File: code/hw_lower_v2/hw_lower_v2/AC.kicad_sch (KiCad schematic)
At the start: 39 parts, among them K1 AHES4191, Q1 BSS138, Q2 BSS138, Q3 BSS138, T1 TS3193-2C 2mA/2mA, U1 BRCS02C, U2 BL0942

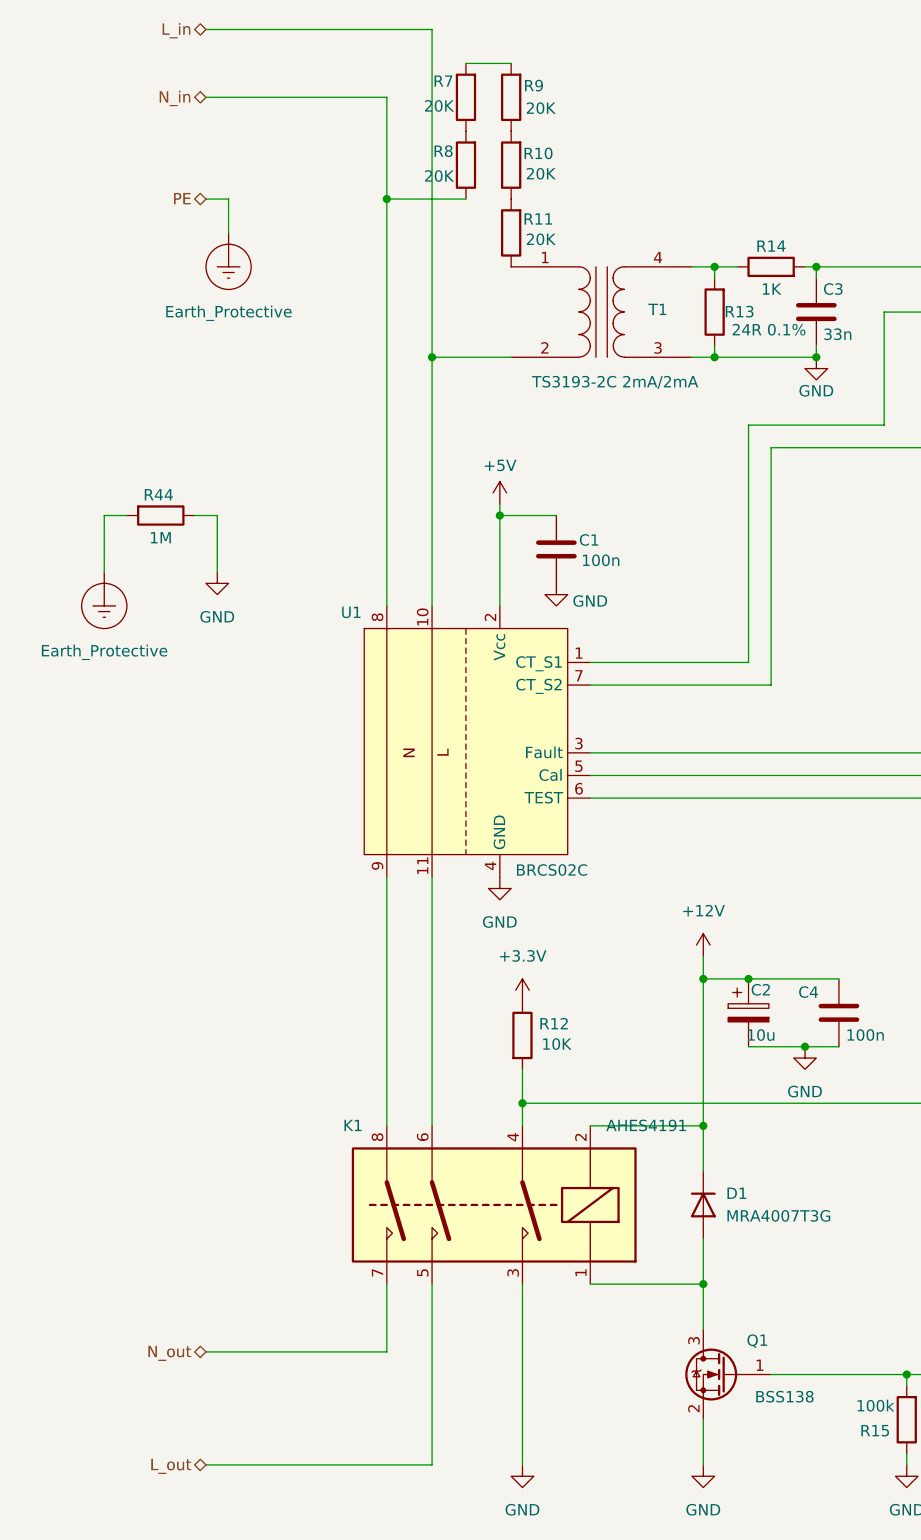
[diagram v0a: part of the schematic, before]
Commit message: further placement and pin relocation
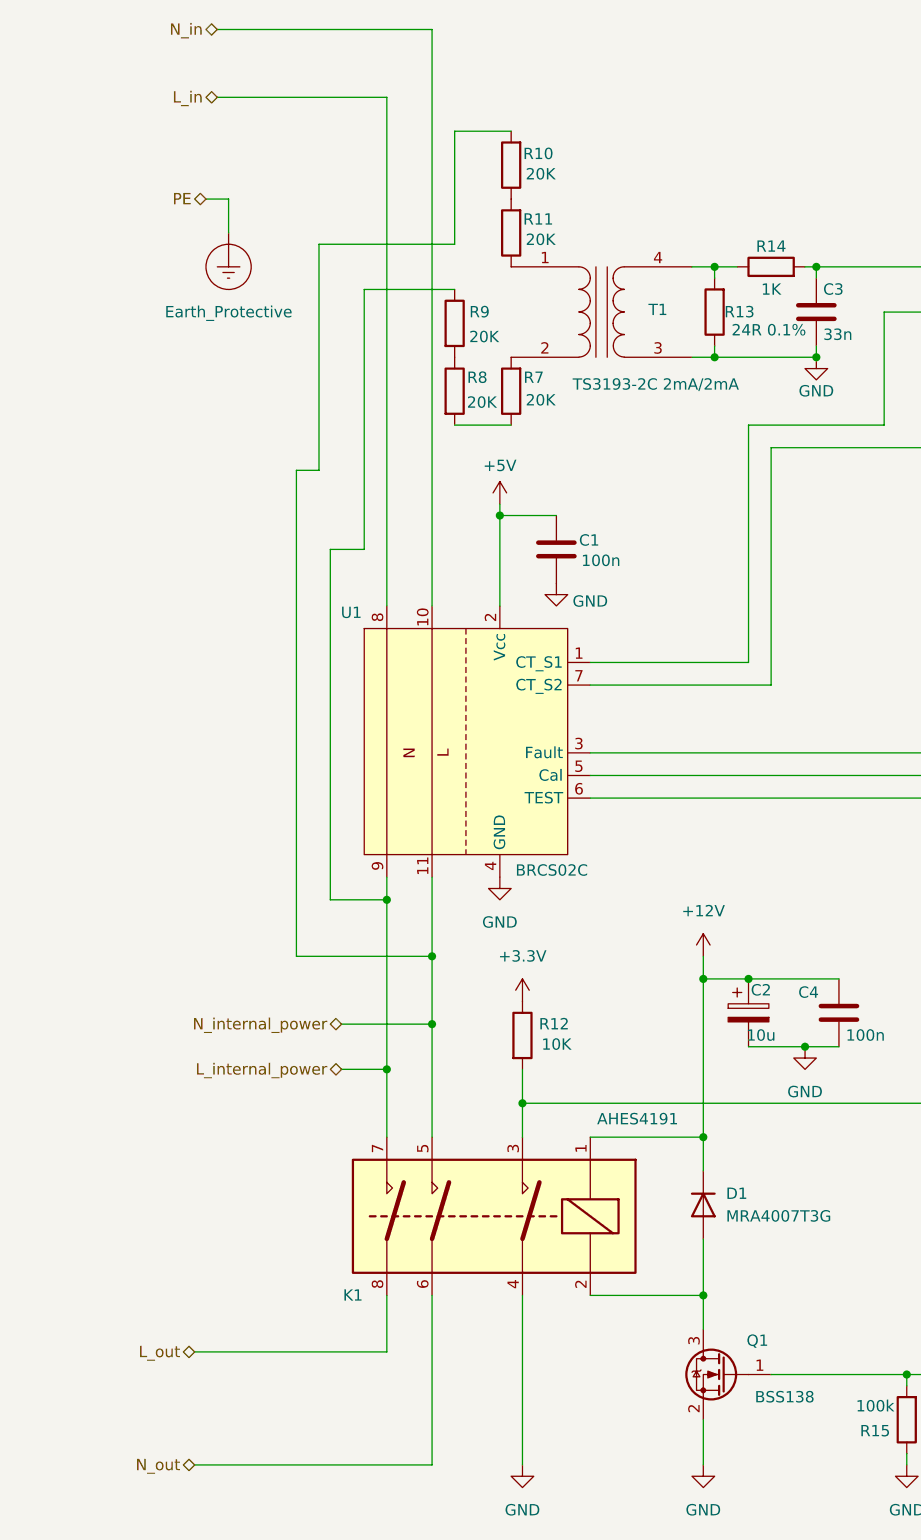
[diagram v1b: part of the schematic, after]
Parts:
- removed R44: 1M, Resistor_SMD:R_1206_3216Metric, symbol Device:R
- U1: footprint multi_new:BRCS02C_1 -> multi_new:BRCS02C_2
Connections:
- net +12V: now also K1.1; no longer K1.2
- net AC_RELAY_SENSE: now also K1.3; no longer K1.4
- net GND: now also K1.4; no longer K1.3
- net L_in: now also U1.8; no longer T1.2 (AB), U1.10
- net L_out: now also K1.8; no longer K1.5
- net N_in: now also U1.10; no longer R8.1, U1.8
- net N_out: now also K1.6; no longer K1.7
- net at R9.2: now also R8.1; no longer R7.2
- net at D1.2 (A), Q1.3 (D): now also K1.2; no longer K1.1
- net N_internal_power: now reaches U1.11
- net N_internal_power: now also K1.5, R10.2; no longer K1.6
- net L_internal_power: now reaches U1.9
- net L_internal_power: now also K1.7, R9.1; no longer K1.8
- new net: R7.2, T1.2 (AB)
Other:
- moved on the sheet: K1, R7, R8, R9

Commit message: commit before experimenting
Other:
- moved on the sheet: C1, C3, C5, C6, C7, Q2, Q3, R10, R11, R13, R14, R16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

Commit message: have one project part library
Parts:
- U2: footprint JLCPCB:SSOP-10_L4.9-W3.9-P1.00-LS6.0-BL -> multi_new:SSOP-10_L4.9-W3.9-P1.00-LS6.0-BL

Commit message: right before tracks
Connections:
- net L_in: now also U1.10; no longer U1.8
- net L_internal_power: now also K1.5, R10.2, U1.11; no longer K1.7, R9.1, U1.9
- net L_out: now also K1.6; no longer K1.8
- net N_in: now also U1.8; no longer U1.10
- net N_internal_power: now also K1.7, R9.1, U1.9; no longer K1.5, R10.2, U1.11
- net N_out: now also K1.8; no longer K1.6

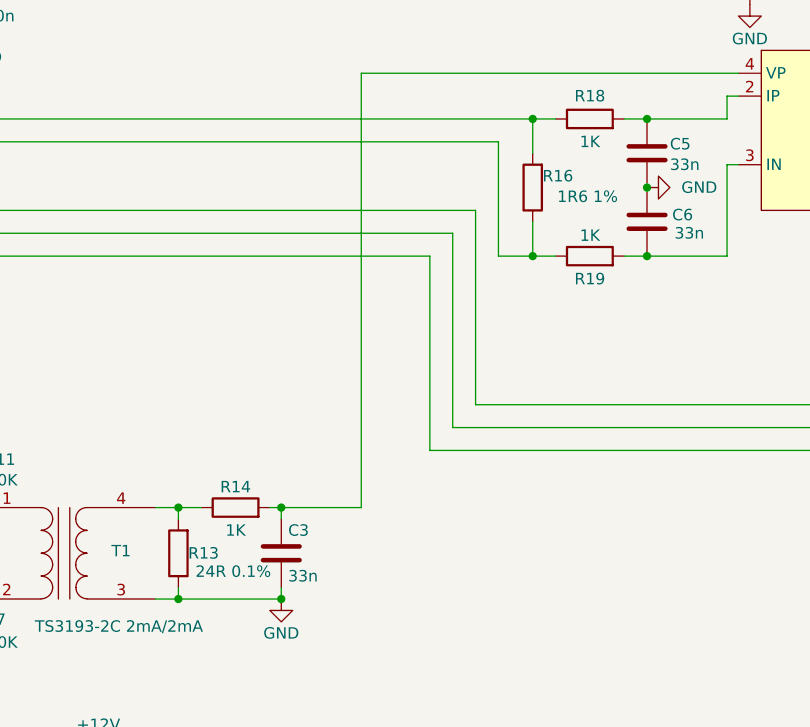
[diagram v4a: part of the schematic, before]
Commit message: moved stuff around a little bit, will optimise the number of components now
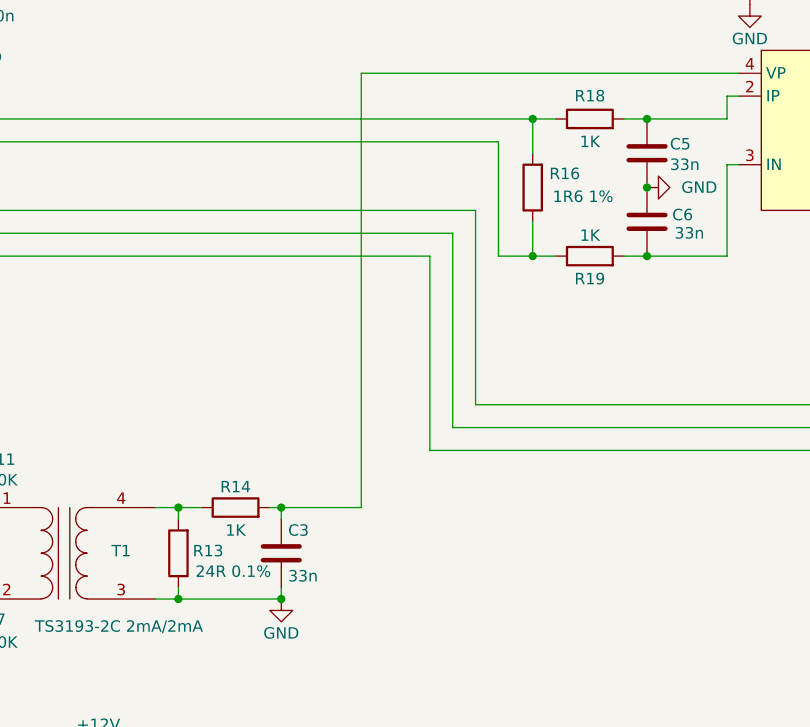
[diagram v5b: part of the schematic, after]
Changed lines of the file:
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@@
 		(dnp no)
 		(property "Reference" "R13"
-			(at 108.204 102.87 0)
+			(at 108.712 102.616 0)
 			(effects
 				(font
@@
 		(dnp no)
 		(property "Reference" "R16"
-			(at 147.574 60.96 0)
+			(at 148.336 60.706 0)
 			(effects
 				(font
@@
 		)
 		(property "Value" "1R6 1%"
-			(at 150.876 63.246 0)
-			(effects
-				(font
+			(at 150.368 63.246 0)
+			(effects
+				(font

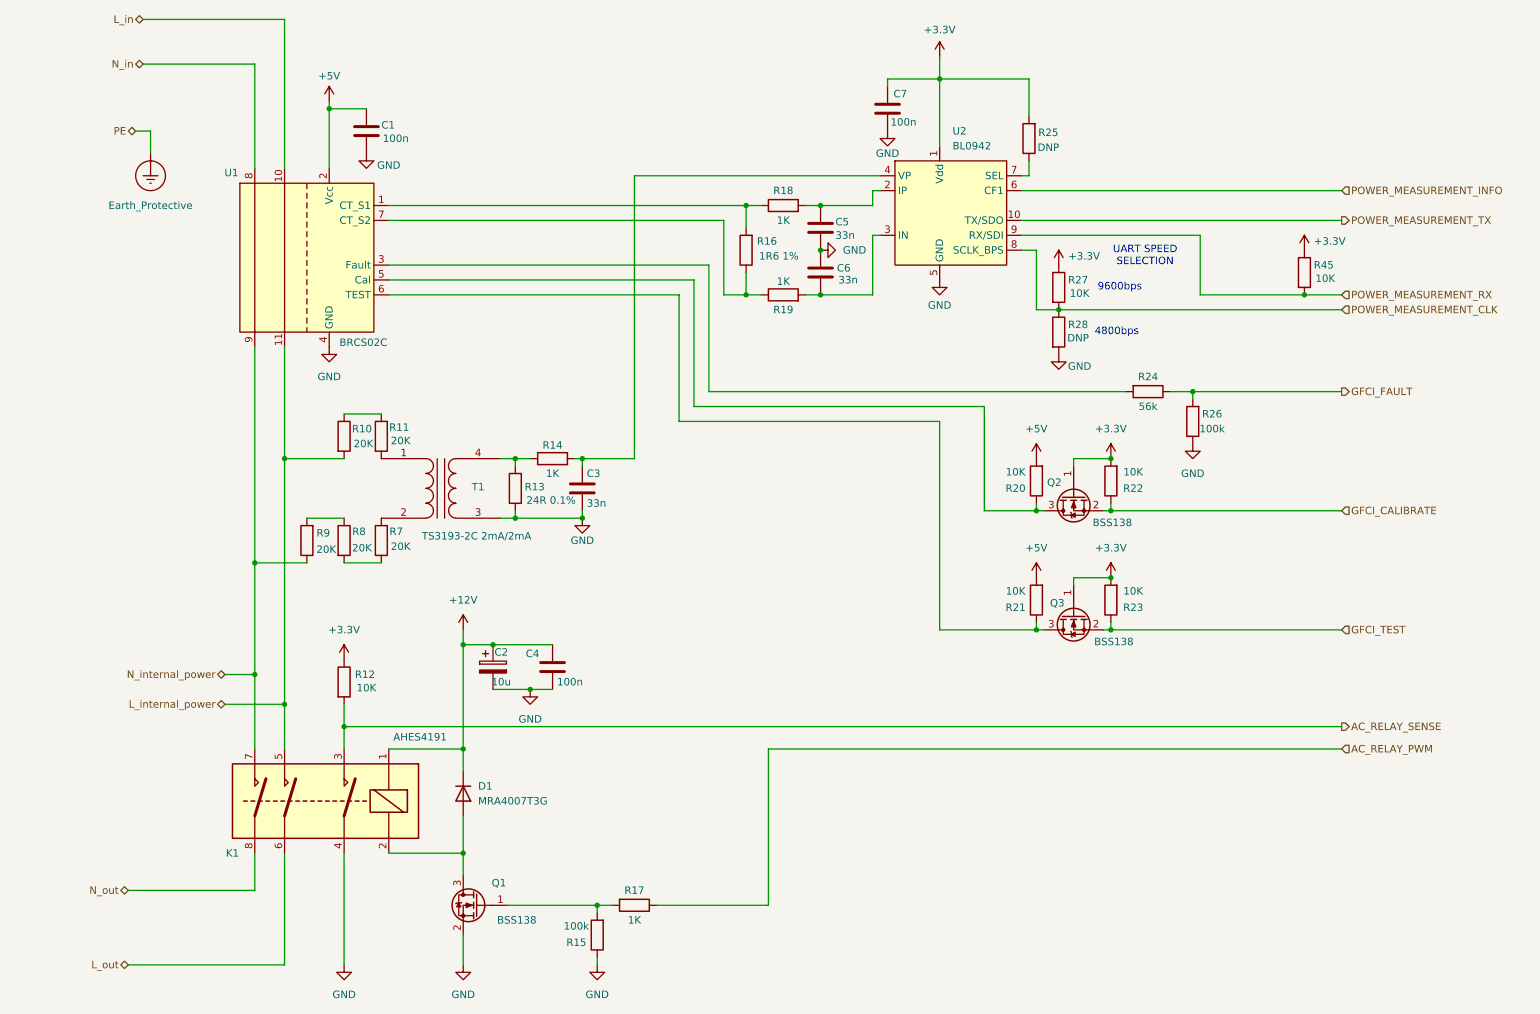
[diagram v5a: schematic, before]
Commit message: simplify component values
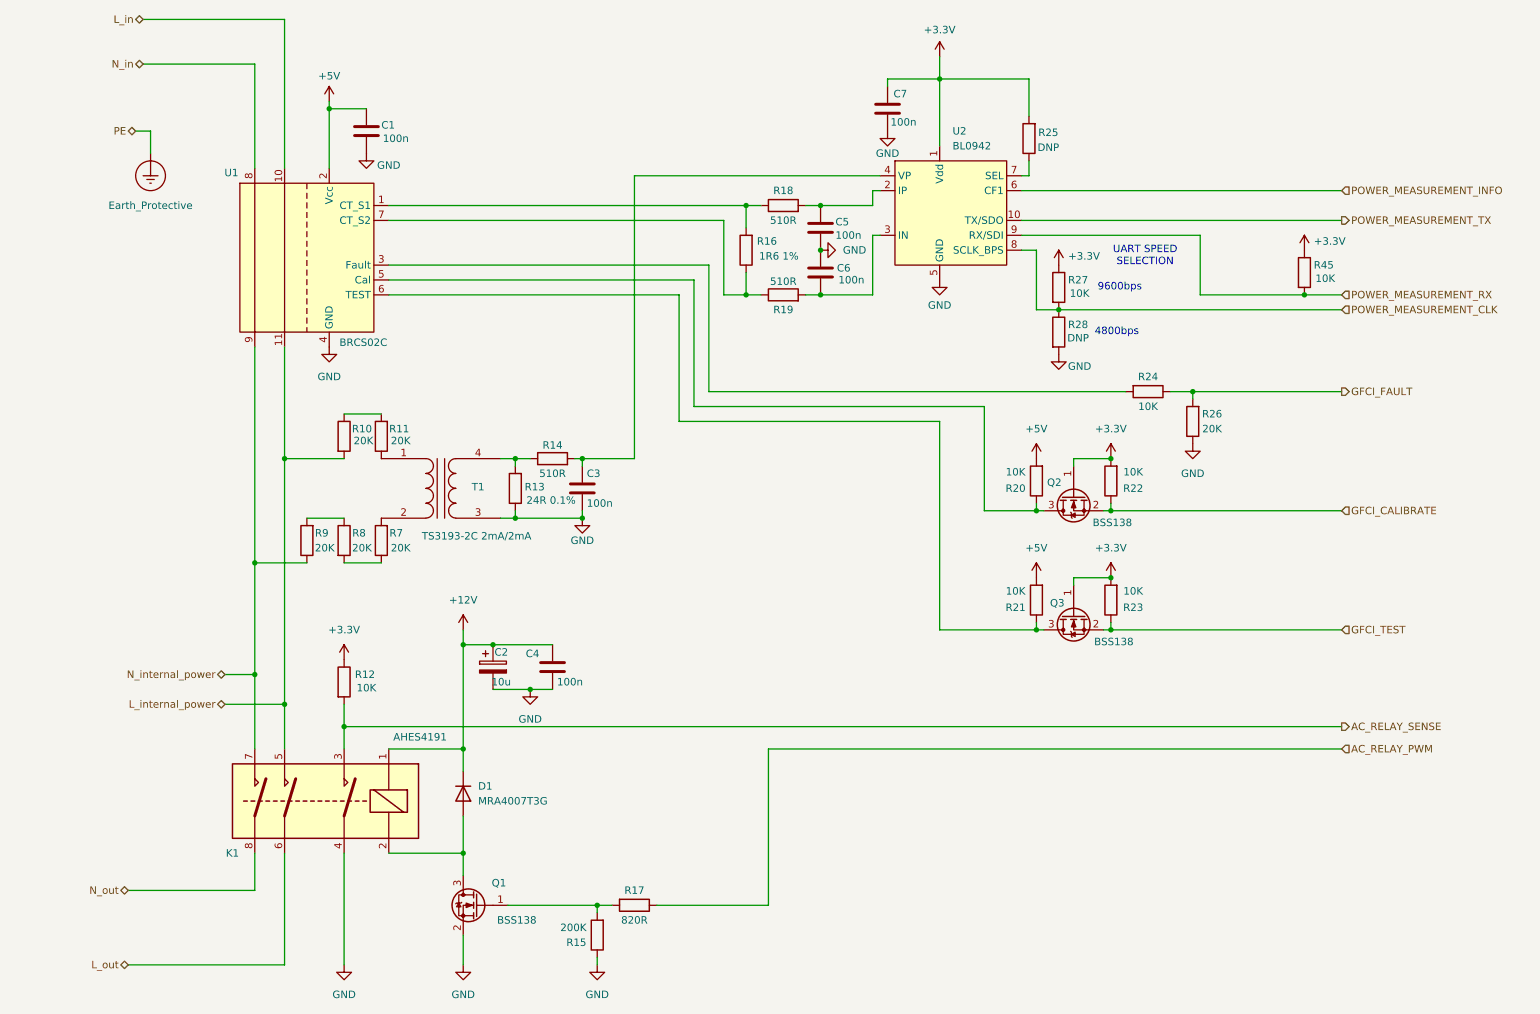
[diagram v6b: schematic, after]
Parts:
- C1, C4, C7: LCSC C38141 -> C327162
- C3, C5, C6: value 33n -> 100n; footprint Capacitor_SMD:C_0603_1608Metric -> Capacitor_SMD:C_0805_2012Metric
- R14, R18, R19: value 1K -> 510R; LCSC C21190 -> C23193
- R15: value 100k -> 200K; LCSC C25804 -> C2989567
- R17: value 1K -> 820R; LCSC C21190 -> C23253
- R24: value 56k -> 10K; LCSC C5250755 -> C25804
- R26: value 100k -> 20K; LCSC C25804 -> C706407
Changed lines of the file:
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@@
 			)
 		)
-		(property "Value" "1K"
+		(property "Value" "820R"
 			(at 125.73 176.53 90)
 			(effects
@@
 			)
 		)
-		(property "LCSC" "C21190"
+		(property "LCSC" "C23253"
 			(at 125.73 173.99 0)
 			(effects
@@
 		(dnp no)
 		(property "Reference" "R8"
-			(at 78.74 110.236 0)
+			(at 78.74 110.49 0)
 			(effects
 				(font
@@
 		(dnp no)
 		(property "Reference" "R7"
-			(at 85.09 110.236 0)
+			(at 85.09 110.49 0)
 			(effects
 				(font
@@
 		)
 		(property "Value" "20K"
-			(at 85.852 112.776 0)
+			(at 85.852 113.03 0)
 			(effects
 				(font
@@
 			)
 		)
-		(property "Value" "56k"
+		(property "Value" "10K"
 			(at 213.36 88.9 90)
 			(effects
@@
 			)
 		)
-		(property "LCSC" "C5250755"
+		(property "LCSC" "C25804"
 			(at 213.36 86.36 0)
 			(effects
@@
 			)
 		)
-		(property "Value" "33n"
+		(property "Value" "100n"
 			(at 160.528 67.31 0)
 			(effects
@@
 			)
 		)
-		(property "Footprint" "Capacitor_SMD:C_0603_1608Metric"
+		(property "Footprint" "Capacitor_SMD:C_0805_2012Metric"
 			(at 158.4452 69.85 0)
 			(effects
@@
 			)
 		)
-		(property "Value" "1K"
+		(property "Value" "510R"
 			(at 111.76 100.33 90)
 			(effects
@@
 			)
 		)
-		(property "LCSC" "C21190"
+		(property "LCSC" "C23193"
 			(at 111.76 97.79 0)
 			(effects
@@
 			)
 		)
-		(property "Value" "33n"
+		(property "Value" "100n"
 			(at 160.02 59.69 0)
 			(effects
@@
 			)
 		)
-		(property "Footprint" "Capacitor_SMD:C_0603_1608Metric"
+		(property "Footprint" "Capacitor_SMD:C_0805_2012Metric"
 			(at 158.4452 62.23 0)
 			(effects
@@
 			)
 		)
-		(property "LCSC" "C38141"
+		(property "LCSC" "C327162"
 			(at 168.91 38.1 0)
 			(effects
@@
 			)
 		)
-		(property "Value" "100k"
+		(property "Value" "20K"
 			(at 224.282 92.71 0)
 			(effects
@@
 			)
 		)
-		(property "LCSC" "C25804"
+		(property "LCSC" "C706407"
 			(at 220.98 91.44 0)
 			(effects
@@
 		(dnp no)
 		(property "Reference" "R11"
-			(at 85.598 92.456 0)
+			(at 85.598 92.71 0)
 			(effects
 				(font
@@
 			)
 		)
-		(property "Value" "1K"
+		(property "Value" "510R"
 			(at 151.13 67.564 90)
 			(effects
@@
 			)
 		)
-		(property "LCSC" "C21190"
+		(property "LCSC" "C23193"
 			(at 151.13 69.85 0)
 			(effects
@@
 			)
 		)
-		(property "LCSC" "C38141"
+		(property "LCSC" "C327162"
 			(at 111.76 133.35 0)
 			(effects
@@
 			)
 		)
-		(property "Value" "33n"
+		(property "Value" "100n"
 			(at 117.602 105.41 0)
 			(effects
@@
 			)
 		)
-		(property "Footprint" "Capacitor_SMD:C_0603_1608Metric"
+		(property "Footprint" "Capacitor_SMD:C_0805_2012Metric"
 			(at 117.8052 106.68 0)
 			(effects
@@
 		(dnp no)
 		(property "Reference" "R9"
-			(at 72.644 110.49 0)
+			(at 72.39 110.49 0)
 			(effects
 				(font
@@
 		)
 		(property "Value" "20K"
-			(at 73.152 113.284 0)
+			(at 72.898 113.03 0)
 			(effects
 				(font
@@
 			)
 		)
-		(property "LCSC" "C38141"
+		(property "LCSC" "C327162"
 			(at 80.01 41.91 0)
 			(effects
@@
 			)
 		)
-		(property "Value" "100k"
-			(at 115.824 177.546 0)
+		(property "Value" "200K"
+			(at 115.316 177.8 0)
 			(effects
 				(font
@@
 			)
 		)
-		(property "LCSC" "C25804"
+		(property "LCSC" "C2989567"
 			(at 119.38 179.07 0)
 			(effects
@@
 			)
 		)
-		(property "Value" "1K"
+		(property "Value" "510R"
 			(at 151.13 57.15 90)
 			(effects
@@
 			)
 		)
-		(property "LCSC" "C21190"
+		(property "LCSC" "C23193"
 			(at 151.13 54.61 0)
 			(effects
@@
 		)
 		(property "Value" "20K"
-			(at 79.502 95.25 0)
+			(at 79.502 94.742 0)
 			(effects
 				(font
